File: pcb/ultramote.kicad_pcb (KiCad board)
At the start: 2 copper layers, 40 x 42.5 mm, 57 parts, among them J1 SMA-KWE902, J2 SM02B-SRSS-TB, J3 USB-C-XKB_U262-16XN, J5 WST-REDFIT-4P, J6 PJ-242D-SMT, J7 PJ-242D-SMT, Q1 2N7002, Q2 BSS84, SW1 SSSS211603, U1 LoRa-E5, U2 TPS2112APW, U3 MCP73831-5-OT, U4 TLV70233DBVT, U5 CH340N, U6 EL357, U7 EL357

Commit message: Fix various 3D models
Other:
- board text added: "ULTRAMOTE ${REVISION}"
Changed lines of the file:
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@@
   (paper "A4")
   (title_block
-    (date "2023-02-12")
-    (rev "0.2a")
+    (date "2023-05-21")
+    (rev "0.2b")
   )
   (layers
@@
     (pad "MP" smd roundrect (at -1.8 1.875 90) (size 1.2 1.8) (layers "F.Cu" "F.Paste" "F.Mask") (roundrect_rratio 0.208333))
     (pad "MP" smd roundrect (at 1.8 1.875 90) (size 1.2 1.8) (layers "F.Cu" "F.Paste" "F.Mask") (roundrect_rratio 0.208333))
-    (model "${KICAD6_3DMODEL_DIR}/Connector_JST.3dshapes/JST_SH_SM02B-SRSS-TB_1x02-1MP_P1.00mm_Horizontal.wrl"
-      (offset (xyz 0 0 0))
+    (model "${KIPRJMOD}/cad_models/SM02B-SRSS-TB.STEP"
+      (offset (xyz 0 1.5 -0.25))
       (scale (xyz 1 1 1))
-      (rotate (xyz 0 0 0))
+      (rotate (xyz -90 0 0))
     )
   )
@@
     (property "ki_keywords" "cap capacitor")
     (attr smd)
-    (fp_text reference "C12" (at -2.735 -0.125 90) (layer "B.SilkS")
+    (fp_text reference "C12" (at 0 1.5 90) (layer "B.SilkS")
         (effects (font (size 0.8 0.8) (thickness 0.1)) (justify mirror))
     )
@@
     (pad "8" smd roundrect (at 2.625 1.905 90) (size 1.65 0.6) (layers "B.Cu" "B.Paste" "B.Mask") (roundrect_rratio 0.25)
       (net 12 "Net-(U5-V3)") (pinfunction "V3") (pintype "passive"))
-    (model "${KICAD6_3DMODEL_DIR}/Package_SO.3dshapes/SOP-8_3.9x4.9mm_P1.27mm.wrl"
-      (offset (xyz 0 0 0))
+    (model "${KIPRJMOD}/cad_models/sop8.STEP"
+      (offset (xyz 0 0 1.5))
       (scale (xyz 1 1 1))
-      (rotate (xyz 0 0 0))
+      (rotate (xyz -90 0 90))
     )
   )
@@
   (gr_arc (start 87.5 59.5) (mid 88.232233 57.732233) (end 90 57)
     (stroke (width 0.05) (type solid)) (layer "Edge.Cuts"))
+  (gr_text "ULTRAMOTE\n${REVISION}" (at 118.25 74.5) (layer "B.SilkS")
+    (effects (font (size 1 1) (thickness 0.15)) (justify left bottom mirror))
+  )
   (gr_text "JLCJLCJLCJLC" (at 102.5 98.5) (layer "F.SilkS")
     (effects (font (size 1 1) (thickness 0.15)))

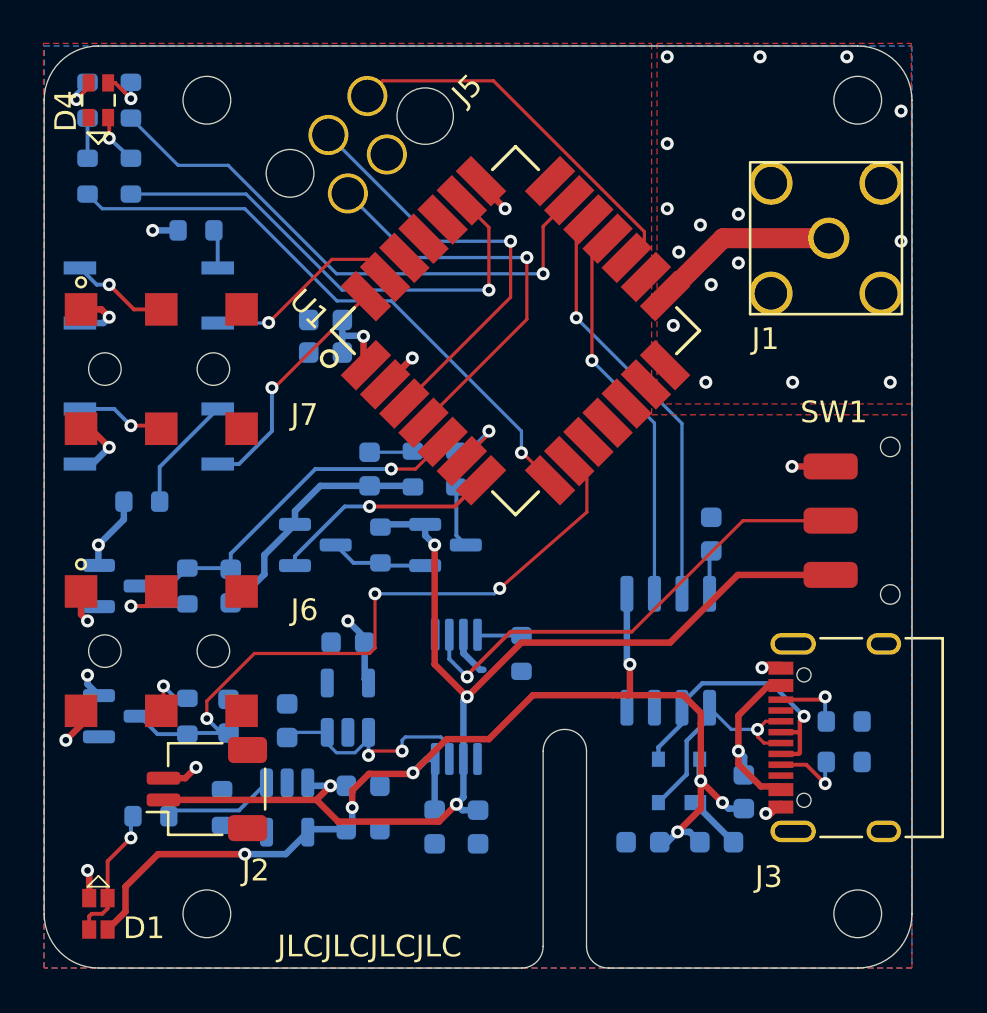
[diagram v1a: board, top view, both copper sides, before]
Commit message: Route Output jack through separate ground
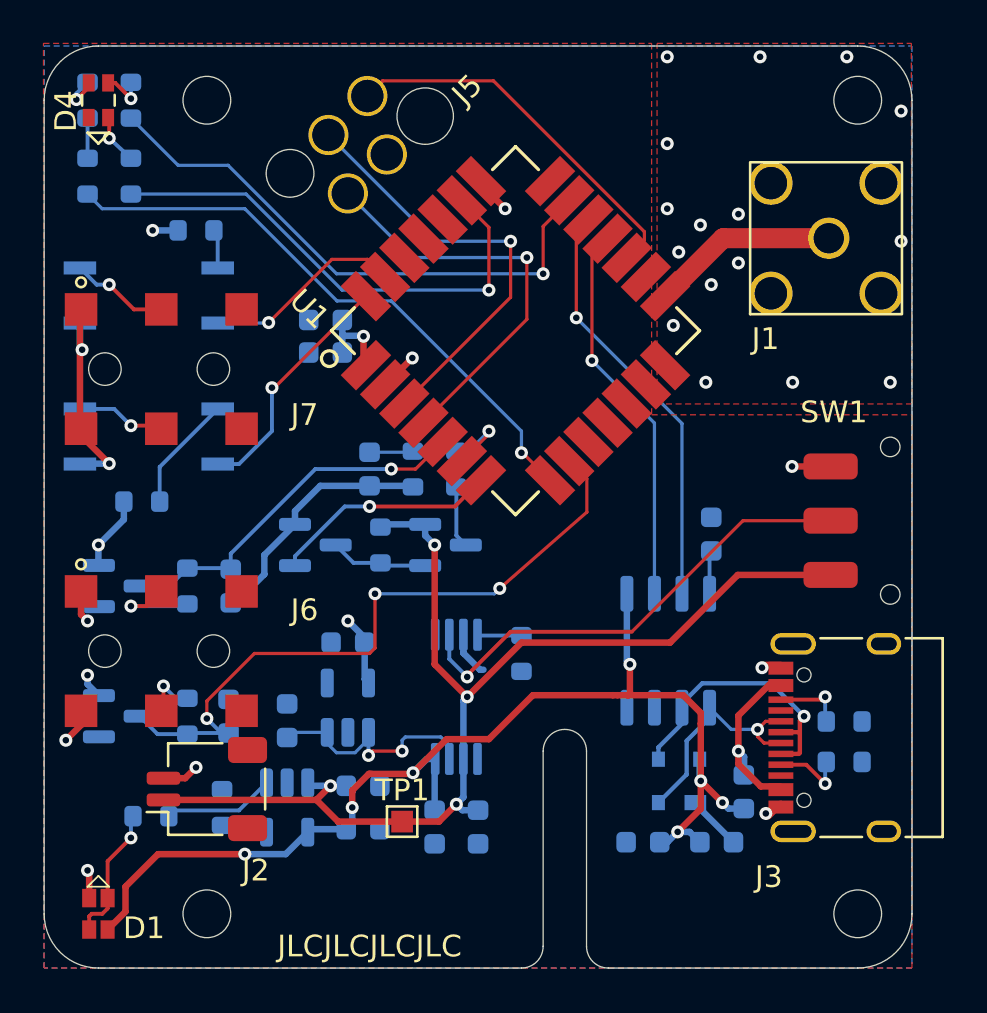
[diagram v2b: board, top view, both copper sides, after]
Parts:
- added TP1: TestPoint, TestPoint:TestPoint_Pad_1.0x1.0mm, F.Cu at (104.0, 92.8)
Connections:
- J7 pad G: GND -> GNDA
- U6 pad 3: GND -> GNDA
- U7 pad 3: GND -> GNDA
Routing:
- net GNDA: track 0.00 -> 10.3 mm, vias 0 -> 2
- net GND: track 35.5 -> 29.3 mm, vias 27 -> 25
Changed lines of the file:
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@@
   (title_block
     (date "2023-05-21")
-    (rev "0.2b")
+    (rev "0.3")
   )
   (layers
@@
   (net 63 "unconnected-(U4-NC-Pad4)")
   (net 64 "unconnected-(U5-~{RTS}-Pad4)")
+  (net 65 "GNDA")
   (footprint "ultramote:lipo403030_300mah" (layer "F.Cu")
     (at 168.03 77.12)
@@
     (pad "" np_thru_hole circle (at 7.8 0) (size 1.5 1.5) (drill 1.5) (layers "*.Cu" "*.Mask"))
     (pad "G" smd rect (at 1.7 -2.75) (size 1.5 1.5) (layers "F.Cu" "F.Paste" "F.Mask")
-      (net 2 "GND") (pintype "passive"))
+      (net 65 "GNDA") (pintype "passive"))
     (pad "G" smd rect (at 1.7 2.75) (size 1.5 1.5) (layers "F.Cu" "F.Paste" "F.Mask")
-      (net 2 "GND") (pintype "passive"))
+      (net 65 "GNDA") (pintype "passive"))
     (pad "S" smd rect (at 5.4 -2.75) (size 1.5 1.5) (layers "F.Cu" "F.Paste" "F.Mask")
       (net 53 "Net-(J7-PadS)") (pintype "passive"))
@@
     (property "ki_description" "Mounting Hole without connection")
     (property "ki_keywords" "mounting hole")
-    (attr exclude_from_pos_files exclude_from_bom)
+    (attr exclude_from_pos_files)
     (fp_text reference "H2" (at 0 -3.2) (layer "F.SilkS") hide
         (effects (font (size 1 1) (thickness 0.15)))
@@
     (pad "" np_thru_hole circle (at 0 0) (size 2.2 2.2) (drill 2.2) (layers "*.Cu" "*.Mask"))
   )
+  (footprint "TestPoint:TestPoint_Pad_1.0x1.0mm" (layer "F.Cu")
+    (at 104 92.75)
+    (descr "SMD rectangular pad as test Point, square 1.0mm side length")
+    (tags "test point SMD pad rectangle square")
+    (property "Sheetfile" "power.kicad_sch")
+    (property "Sheetname" "power")
+    (property "ki_description" "test point")
+    (property "ki_keywords" "test point tp")
+    (attr exclude_from_pos_files)
+    (fp_text reference "TP1" (at 0 -1.448) (layer "F.SilkS")
+        (effects (font (size 1 1) (thickness 0.15)))
+    )
+    (fp_text value "TestPoint" (at 0 1.55) (layer "F.Fab")
+        (effects (font (size 1 1) (thickness 0.15)))
+    )
+    (fp_text user "${REFERENCE}" (at 0 -1.45) (layer "F.Fab")
+        (effects (font (size 1 1) (thickness 0.15)))
+    )
+    (fp_line (start -0.7 -0.7) (end 0.7 -0.7)
+      (stroke (width 0.12) (type solid)) (layer "F.SilkS"))
+    (fp_line (start -0.7 0.7) (end -0.7 -0.7)
+      (stroke (width 0.12) (type solid)) (layer "F.SilkS"))
+    (fp_line (start 0.7 -0.7) (end 0.7 0.7)
+      (stroke (width 0.12) (type solid)) (layer "F.SilkS"))
+    (fp_line (start 0.7 0.7) (end -0.7 0.7)
+      (stroke (width 0.12) (type solid)) (layer "F.SilkS"))
+    (fp_line (start -1 -1) (end -1 1)
+      (stroke (width 0.05) (type solid)) (layer "F.CrtYd"))
+    (fp_line (start -1 -1) (end 1 -1)
+      (stroke (width 0.05) (type solid)) (layer "F.CrtYd"))
+    (fp_line (start 1 1) (end -1 1)
+      (stroke (width 0.05) (type solid)) (layer "F.CrtYd"))
+    (fp_line (start 1 1) (end 1 -1)
+      (stroke (width 0.05) (type solid)) (layer "F.CrtYd"))
+    (pad "1" smd rect (at 0 0) (size 1 1) (layers "F.Cu" "F.Mask")
+      (net 3 "+BATT") (pinfunction "1") (pintype "passive"))
+  )
   (footprint "ultramote:19-237-R6GHBHC-A01-2T" (layer "F.Cu")
     (at 90 59.5 -90)
@@
     (property "ki_description" "Mounting Hole without connection")
     (property "ki_keywords" "mounting hole")
-    (attr exclude_from_pos_files exclude_from_bom)
+    (attr exclude_from_pos_files)
     (fp_text reference "H3" (at 0 -3.2) (layer "F.SilkS") hide
         (effects (font (size 1 1) (thickness 0.15)))
@@
     (property "ki_description" "Mounting Hole without connection")
     (property "ki_keywords" "mounting hole")
-    (attr exclude_from_pos_files exclude_from_bom)
+    (attr exclude_from_pos_files)
     (fp_text reference "H1" (at 0 -3.2) (layer "F.SilkS") hide
         (effects (font (size 1 1) (thickness 0.15)))
@@
     (property "ki_description" "Mounting Hole without connection")
     (property "ki_keywords" "mounting hole")
-    (attr exclude_from_pos_files exclude_from_bom)
+    (attr exclude_from_pos_files)
     (fp_text reference "H4" (at 0 -3.2) (layer "F.SilkS") hide
         (effects (font (size 1 1) (thickness 0.15)))
@@
       (net 49 "/OUTPUT_TIP") (pintype "passive"))
     (pad "3" smd rect (at 3.175 -1.27 270) (size 0.6 1.5) (layers "B.Cu" "B.Paste" "B.Mask")
-      (net 2 "GND") (pintype "passive"))
+      (net 65 "GNDA") (pintype "passive"))
     (pad "4" smd rect (at 3.175 1.27 270) (size 0.6 1.5) (layers "B.Cu" "B.Paste" "B.Mask")
       (net 55 "Net-(J7-PadT)") (pintype "passive"))
@@
       (net 48 "/OUTPUT_SLEEVE") (pintype "passive"))
     (pad "3" smd rect (at 3.175 -1.27 270) (size 0.6 1.5) (layers "B.Cu" "B.Paste" "B.Mask")
-      (net 2 "GND") (pintype "passive"))
+      (net 65 "GNDA") (pintype "passive"))
     (pad "4" smd rect (at 3.175 1.27 270) (size 0.6 1.5) (layers "B.Cu" "B.Paste" "B.Mask")
       (net 53 "Net-(J7-PadS)") (pintype "passive"))
@@
   (segment (start 107.636369 63.386369) (end 108.75 64.5) (width 0.3) (layer "F.Cu") (net 2))
   (segment (start 94 90.75) (end 94.5 90.25) (width 0.3) (layer "F.Cu") (net 2))
-  (segment (start 89.2 69.141804) (end 90.141804 69.141804) (width 0.3) (layer "F.Cu") (net 2))
   (segment (start 103.216951 72.597515) (end 103.252485 72.597515) (width 0.3) (layer "F.Cu") (net 2))
-  (segment (start 89.641804 74.641804) (end 90.5 75.5) (width 0.3) (layer "F.Cu") (net 2))
-  (segment (start 89.2 74.641804) (end 89.641804 74.641804) (width 0.3) (layer "F.Cu") (net 2))
   (segment (start 89.575 96.275) (end 89.575 95.075) (width 0.3) (layer "F.Cu") (net 2))
-  (segment (start 90.141804 69.141804) (end 90.5 69.5) (width 0.3) (layer "F.Cu") (net 2))
   (segment (start 103.252485 72.597515) (end 104.47 71.38) (width 0.3) (layer "F.Cu") (net 2))
   (segment (start 121.458461 85.528938) (end 120.574601 85.528938) (width 0.3) (layer "F.Cu") (net 2))
@@
   (via (at 104.47 71.38) (size 0.6) (drill 0.3) (layers "F.Cu" "B.Cu") (net 2))
   (via (at 116.22 57.5) (size 0.6) (drill 0.3) (layers "F.Cu" "B.Cu") (free) (net 2))
-  (via (at 90.5 75.5) (size 0.6) (drill 0.3) (layers "F.Cu" "B.Cu") (net 2))
   (via (at 122 72.5) (size 0.6) (drill 0.3) (layers "F.Cu" "B.Cu") (free) (net 2))
   (via (at 120.5 57.5) (size 0.6) (drill 0.3) (layers "F.Cu" "B.Cu") (free) (net 2))
@@
   (via (at 116.75 66.5) (size 0.6) (drill 0.3) (layers "F.Cu" "B.Cu") (free) (net 2))
   (via (at 126.5 72.5) (size 0.6) (drill 0.3) (layers "F.Cu" "B.Cu") (free) (net 2))
-  (via (at 90.5 69.5) (size 0.6) (drill 0.3) (layers "F.Cu" "B.Cu") (net 2))
   (via (at 124.5 57.5) (size 0.6) (drill 0.3) (layers "F.Cu" "B.Cu") (free) (net 2))
   (via (at 127 66) (size 0.6) (drill 0.3) (layers "F.Cu" "B.Cu") (free) (net 2))
@@
   (segment (start 106.825 84.1375) (end 106.825 84.987229) (width 0.3) (layer "B.Cu") (net 2))
   (segment (start 117.515 91.94) (end 119.275 93.7) (width 0.3) (layer "B.Cu") (net 2))
-  (segment (start 89.15 76.270001) (end 89.729999 76.270001) (width 0.3) (layer "B.Cu") (net 2))
   (segment (start 100.225 77.275) (end 102.5 77.275) (width 0.3) (layer "B.Cu") (net 2))
   (segment (start 102.5 77.275) (end 104.45 77.275) (width 0.3) (layer "B.Cu") (net 2))
   (segment (start 96.333196 82.666804) (end 96.1 82.666804) (width 0.3) (layer "B.Cu") (net 2))
   (segment (start 117.515 91.875) (end 117.515 91.94) (width 0.3) (layer "B.Cu") (net 2))
-  (segment (start 90.229999 69.770001) (end 90.5 69.5) (width 0.3) (layer "B.Cu") (net 2))
   (segment (start 99.0625 78.4375) (end 100.225 77.275) (width 0.3) (layer "B.Cu") (net 2))
   (segment (start 107.587771 85.75) (end 107.75 85.75) (width 0.3) (layer "B.Cu") (net 2))
@@
   (segment (start 99.0625 79.05) (end 99.0625 78.4375) (width 0.3) (layer "B.Cu") (net 2))
   (segment (start 97.65 81.35) (end 96.333196 82.666804) (width 0.3) (layer "B.Cu") (net 2))
-  (segment (start 89.15 69.770001) (end 90.229999 69.770001) (width 0.3) (layer "B.Cu") (net 2))
-  (segment (start 89.729999 76.270001) (end 90.5 75.5) (width 0.3) (layer "B.Cu") (net 2))
   (segment (start 97.65 80.4625) (end 97.65 81.35) (width 0.3) (layer "B.Cu") (net 2))
   (segment (start 104.45 77.275) (end 104.5 77.325) (width 0.3) (layer "B.Cu") (net 2))
@@
   (segment (start 90.730001 73.730001) (end 91.5 74.5) (width 0.18) (layer "B.Cu") (net 55))
   (segment (start 89.15 73.730001) (end 90.730001 73.730001) (width 0.18) (layer "B.Cu") (net 55))
+  (segment (start 89.2 74.95) (end 90.5 76.25) (width 0.3) (layer "F.Cu") (net 65))
+  (segment (start 89.15 69.191804) (end 89.15 74.591804) (width 0.3) (layer "F.Cu") (net 65))
+  (segment (start 89.2 69.141804) (end 89.15 69.191804) (width 0.3) (layer "F.Cu") (net 65))
+  (segment (start 89.2 74.641804) (end 89.2 74.95) (width 0.3) (layer "F.Cu") (net 65))
+  (segment (start 89.15 74.591804) (end 89.2 74.641804) (width 0.3) (layer "F.Cu") (net 65))
+  (via (at 89.25 71) (size 0.6) (drill 0.3) (layers "F.Cu" "B.Cu") (net 65))
+  (via (at 90.5 76.25) (size 0.6) (drill 0.3) (layers "F.Cu" "B.Cu") (net 65))
+  (segment (start 89.15 69.770001) (end 89.15 70.9) (width 0.3) (layer "B.Cu") (net 65))
+  (segment (start 89.15 70.9) (end 89.25 71) (width 0.3) (layer "B.Cu") (net 65))
+  (segment (start 90.5 76.25) (end 89.170001 76.25) (width 0.3) (layer "B.Cu") (net 65))
+  (segment (start 89.170001 76.25) (end 89.15 76.270001) (width 0.3) (layer "B.Cu") (net 65))
   (zone (net 2) (net_name "GND") (layer "F.Cu") (hatch edge 0.508)
     (connect_pads (clearance 0))
